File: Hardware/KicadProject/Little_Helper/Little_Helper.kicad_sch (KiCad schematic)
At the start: 37 parts, among them J1 USB_B_Micro_Molex_1050171001_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, J2 Conn_01x02_Pin, Q1 DMG3415U, SW1 SW_Push, SW2 SW_Push, SW3 SW_Push, SW4 SW_Push, SW5 SW_Push, SW6 SW_SPST, SW7 SW_Push, SW8 SW_Push, U1 AP2112K-3.3, U2 ESP32-S3-MINI-1, U3 MCP73831-2-OT

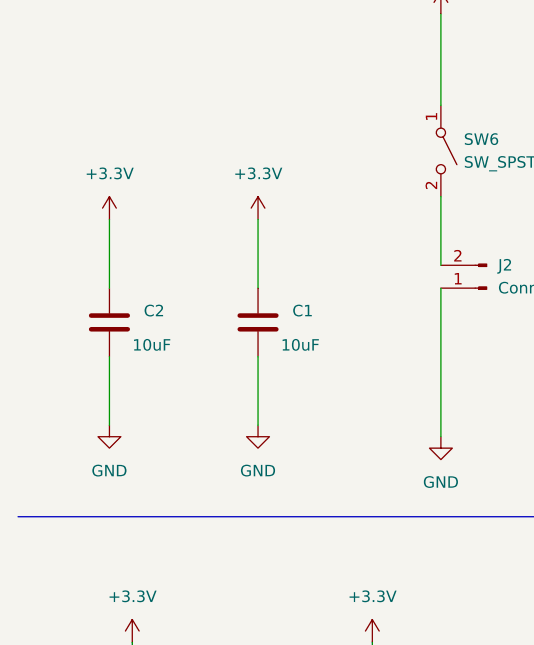
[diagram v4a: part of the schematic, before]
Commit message: 10uf cap from 0603 to 0805
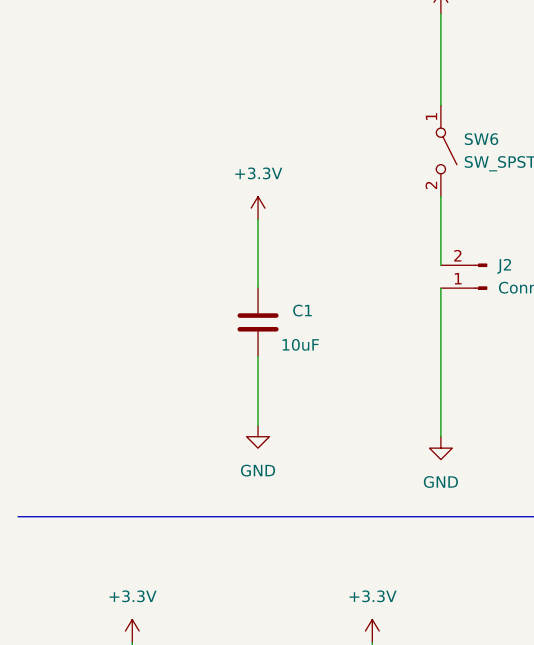
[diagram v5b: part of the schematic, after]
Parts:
- removed C2: 10uF, Capacitor_SMD:C_0603_1608Metric, symbol PCM_Capacitor_AKL:C_0603
- C6: footprint Capacitor_SMD:C_0603_1608Metric -> Capacitor_SMD:C_0805_2012Metric
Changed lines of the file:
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@@
 	(wire
 		(pts
-			(xy 22.86 127) (xy 22.86 134.62)
-		)
-		(stroke
-			(width 0)
-			(type default)
-		)
-	)
-	(wire
-		(pts
 			(xy 77.47 45.72) (xy 77.47 54.61)
 		)
@@
 	(wire
 		(pts
-			(xy 22.86 111.76) (xy 22.86 119.38)
-		)
-		(stroke
-			(width 0)
-			(type default)
-		)
-	)
-	(wire
-		(pts
 			(xy 63.5 25.4) (xy 72.39 25.4)
 		)
@@
 	)
 	(symbol
-		(lib_id "power:+3.3V")
-		(at 22.86 111.76 0)
-		(unit 1)
-		(exclude_from_sim no)
-		(in_bom yes)
-		(on_board yes)
-		(dnp no)
-		(fields_autoplaced yes)
-		(property "Reference" "#PWR07"
-			(at 22.86 115.57 0)
-			(effects
-				(font
-					(size 1.27 1.27)
-				)
-				(hide yes)
-			)
-		)
-		(property "Value" "+3.3V"
-			(at 22.86 106.68 0)
-			(effects
-				(font
-					(size 1.27 1.27)
-				)
-			)
-		)
-		(property "Footprint" ""
-			(at 22.86 111.76 0)
-			(effects
-				(font
-					(size 1.27 1.27)
-				)
-				(hide yes)
-			)
-		)
-		(property "Datasheet" ""
-			(at 22.86 111.76 0)
-			(effects
-				(font
-					(size 1.27 1.27)
-				)
-				(hide yes)
-			)
-		)
-		(property "Description" "Power symbol creates a global label with name \"+3.3V\""
-			(at 22.86 111.76 0)
-			(effects
-				(font
-					(size 1.27 1.27)
-				)
-				(hide yes)
-			)
-		)
-		(pin "1"
-		)
-		(instances
-			(project "Little_Helper"
-				(path "/be456eed-bb99-4947-8d6f-815aa9683d71"
-					(reference "#PWR07")
-					(unit 1)
-				)
-			)
-		)
-	)
-	(symbol
 		(lib_id "Device:R")
 		(at 139.7 30.48 0)
@@
 	)
 	(symbol
-		(lib_id "PCM_Capacitor_AKL:C_0603")
-		(at 22.86 123.19 0)
-		(unit 1)
-		(exclude_from_sim no)
-		(in_bom yes)
-		(on_board yes)
-		(dnp no)
-		(property "Reference" "C2"
-			(at 26.67 121.9199 0)
-			(effects
-				(font
-					(size 1.27 1.27)
-				)
-				(justify left)
-			)
-		)
-		(property "Value" "10uF"
-			(at 25.4 125.73 0)
-			(effects
-				(font
-					(size 1.27 1.27)
-				)
-				(justify left)
-			)
-		)
-		(property "Footprint" "Capacitor_SMD:C_0603_1608Metric"
-			(at 23.8252 127 0)
-			(effects
-				(font
-					(size 1.27 1.27)
-				)
-				(hide yes)
-			)
-		)
-		(property "Datasheet" "~"
-			(at 22.86 123.19 0)
-			(effects
-				(font
-					(size 1.27 1.27)
-				)
-				(hide yes)
-			)
-		)
-		(property "Description" "SMD 0603 MLCC capacitor, Alternate KiCad Library"
-			(at 22.86 123.19 0)
-			(effects
-				(font
-					(size 1.27 1.27)
-				)
-				(hide yes)
-			)
-		)
-		(pin "2"
-		)
-		(pin "1"
-		)
-		(instances
-			(project "Little_Helper"
-				(path "/be456eed-bb99-4947-8d6f-815aa9683d71"
-					(reference "C2")
-					(unit 1)
-				)
-			)
-		)
-	)
-	(symbol
 		(lib_id "ba_diode:BAS16")
 		(at 76.2 25.4 0)
@@
 			)
 		)
-		(property "Footprint" "Capacitor_SMD:C_0603_1608Metric"
+		(property "Footprint" "Capacitor_SMD:C_0805_2012Metric"
 			(at 258.7752 101.6 0)
 			(effects
@@
 					(unit 1)
 				)
-			)
-		)
-	)
-	(symbol
-		(lib_id "power:GND")
-		(at 22.86 134.62 0)
-		(unit 1)
-		(exclude_from_sim no)
-		(in_bom yes)
-		(on_board yes)
-		(dnp no)
-		(fields_autoplaced yes)
-		(property "Reference" "#PWR014"
-			(at 22.86 140.97 0)
-			(effects
-				(font
-					(size 1.27 1.27)
-				)
-				(hide yes)
-			)
-		)
-		(property "Value" "GND"
-			(at 22.86 139.7 0)
-			(effects
-				(font
-					(size 1.27 1.27)
-				)
-			)
-		)
-		(property "Footprint" ""
-			(at 22.86 134.62 0)
-			(effects
-				(font
-					(size 1.27 1.27)
-				)
-				(hide yes)
-			)
-		)
-		(property "Datasheet" ""
-			(at 22.86 134.62 0)
-			(effects
-				(font
-					(size 1.27 1.27)
-				)
-				(hide yes)
-			)
-		)
-		(property "Description" "Power symbol creates a global label with name \"GND\" , ground"
-			(at 22.86 134.62 0)
-			(effects
-				(font
-					(size 1.27 1.27)
-				)
-				(hide yes)
-			)
-		)
-		(pin "1"
-		)
-		(instances
-			(project "Little_Helper"
-				(path "/be456eed-bb99-4947-8d6f-815aa9683d71"
-					(reference "#PWR014")
-					(unit 1)
-				)

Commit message: add lsc parts
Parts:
- C1, C3, C4, C5, C6, C8: LCSC (none) -> C1713
- C7, C9: LCSC (none) -> C1592
- D1: LCSC (none) -> C78545
- D2: LCSC (none) -> C2286
- D3: LCSC (none) -> C2843785
- D4: LCSC (none) -> C79997
- J1: LCSC (none) -> C505111
- J2: LCSC (none) -> C145970
- R1, R10, R11: LCSC (none) -> C115316
- R3, R4: LCSC (none) -> C149504
- R5, R6, R7, R8, R9: LCSC (none) -> C17414
- U1: LCSC (none) -> C51118
- U2: LCSC (none) -> C2913206
- U3: LCSC (none) -> C424093

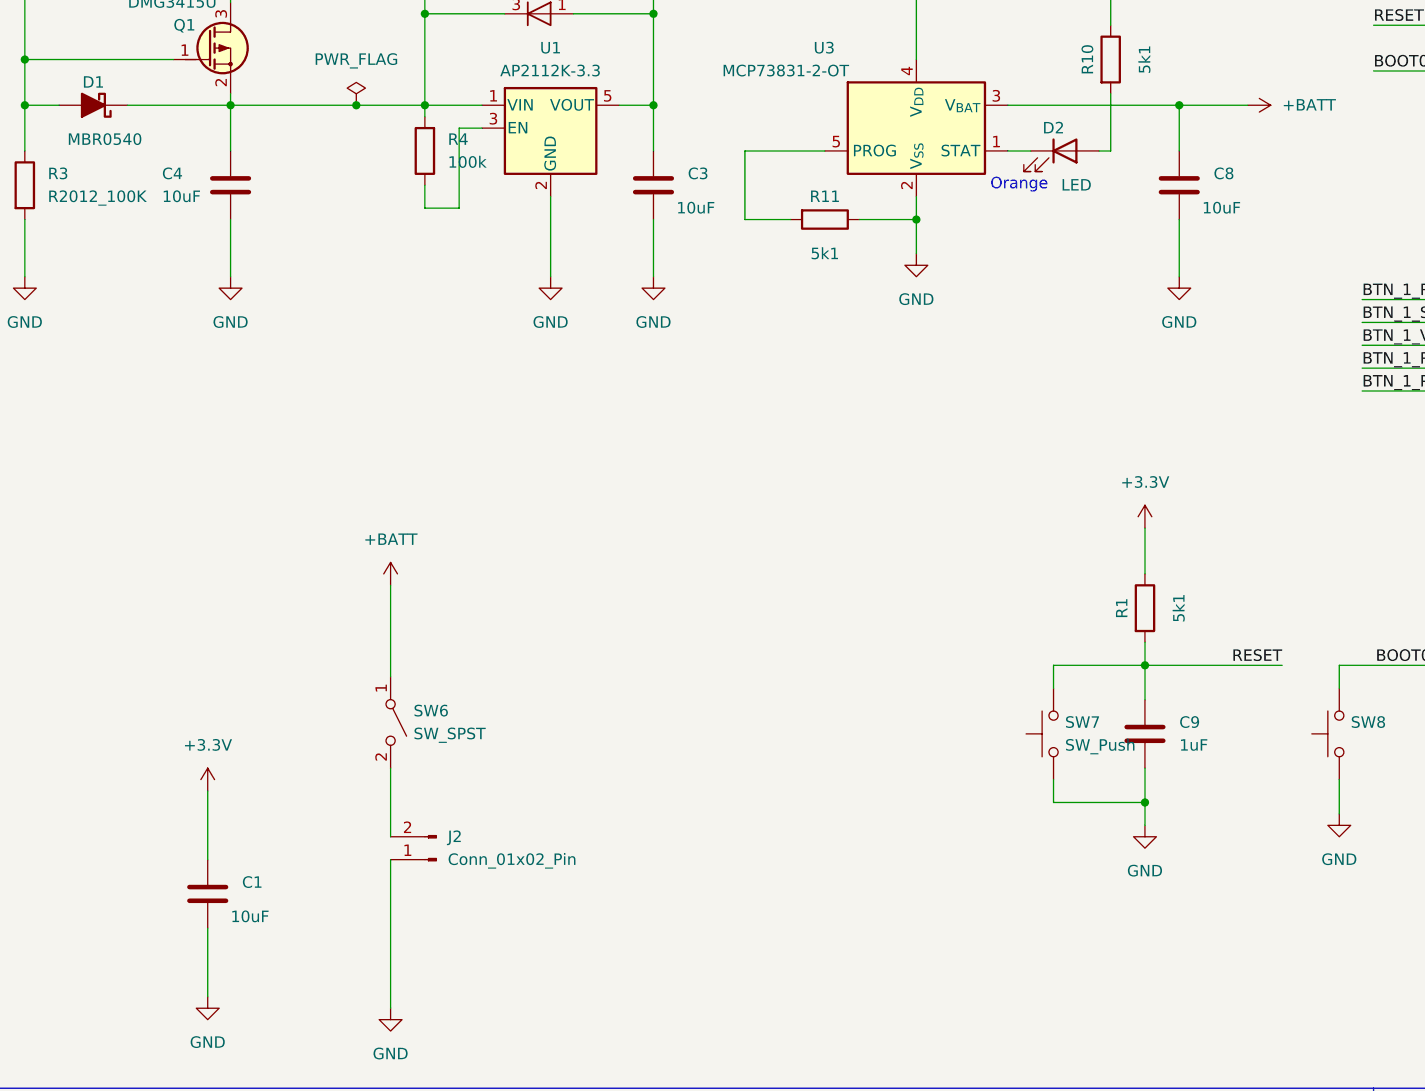
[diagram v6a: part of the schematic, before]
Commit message: select the right footprint
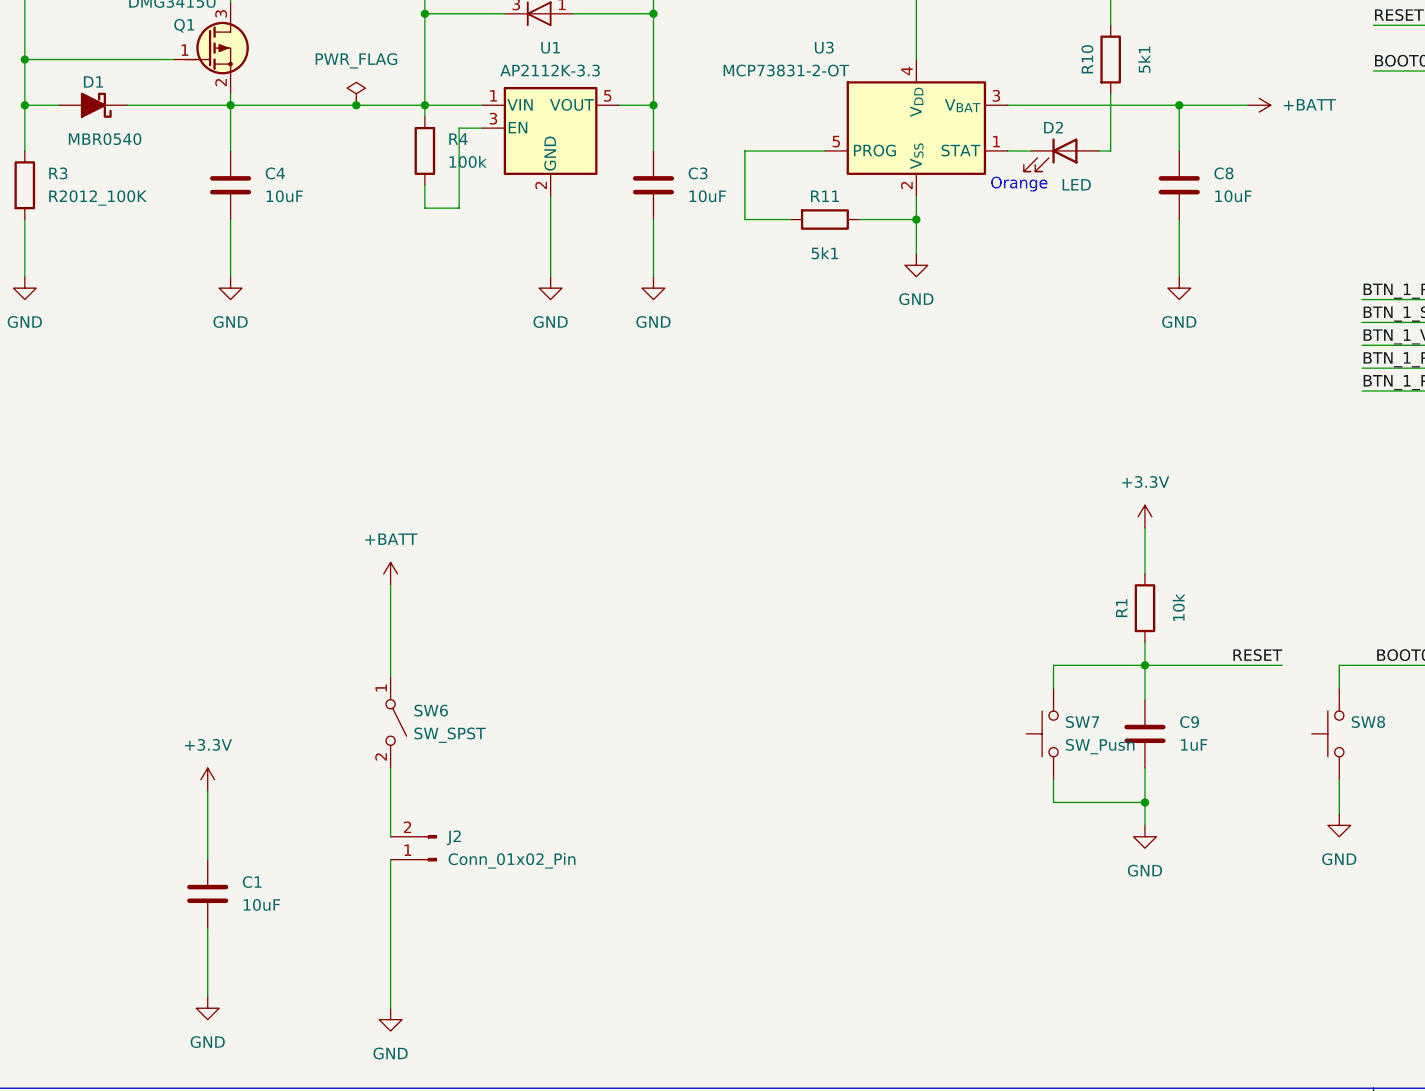
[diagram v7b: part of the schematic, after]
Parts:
- removed C1, C3, C4, C5, C8: 10uF, Capacitor_SMD:C_0603_1608Metric, symbol PCM_Capacitor_AKL:C_0603
- removed C6: 10uF, Capacitor_SMD:C_0805_2012Metric, symbol PCM_Capacitor_AKL:C_0603
- added C1, C3, C4, C5, C6, C8: 10uF, Capacitor_SMD:C_0805_2012Metric, symbol PCM_Capacitor_US_AKL:C_0805
- R1: value 5k1 -> 10k
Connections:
- net +3.3V: now also C1.1, C3.1, C5.1, C6.1
- net +BATT: now also C8.1
- net GND: now also C1.2, C3.2, C4.2, C5.2, C6.2, C8.2
- net NEOPIX_VDD: now also C4.1

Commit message: Change Putton Switch
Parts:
- SW7, SW8: footprint Button_Switch_SMD:SW_Push_1P1T_NO_Vertical_Wuerth_434133025816 -> Button_Switch_SMD:SW_Push_SPST_NO_Alps_SKRK
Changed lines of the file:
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@@
 			)
 		)
-		(property "Footprint" "Button_Switch_SMD:SW_Push_1P1T_NO_Vertical_Wuerth_434133025816"
+		(property "Footprint" "Button_Switch_SMD:SW_Push_SPST_NO_Alps_SKRK"
 			(at 128.27 105.41 0)
 			(effects
@@
 			)
 		)
-		(property "Footprint" "Button_Switch_SMD:SW_Push_1P1T_NO_Vertical_Wuerth_434133025816"
+		(property "Footprint" "Button_Switch_SMD:SW_Push_SPST_NO_Alps_SKRK"
 			(at 160.02 105.41 0)
 			(effects
